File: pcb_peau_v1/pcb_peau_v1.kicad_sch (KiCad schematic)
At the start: 23 parts, among them J1 Conn_01x05, J2 Conn_01x05, J3 Conn_01x16, J4 Conn_01x24, U1 REF200AU, U2 TLC274, U3 CD74HC4067SM, U4 CD74HC4067SM, U5 CD74HC4067SM, U6 CD74HC4067SM, U7 TLC274, U8 TLC274, U9 TLC274

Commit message: Schématic
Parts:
- added H1, H2, H3, H4: MountingHole_Pad, MountingHole:MountingHole_3.2mm_M3_DIN965_Pad, symbol Mechanical:MountingHole_Pad
- J1, J2: footprint (none) -> Connector_JST:JST_EH_B5B-EH-A_1x05_P2.50mm_Vertical
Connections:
- net 0: now also H1.1, H2.1, H3.1, H4.1
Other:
- title: (none) -> PCB PEAU
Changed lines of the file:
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@@
 (kicad_sch (version 20230121) (generator eeschema)
   (paper "A3")
+  (title_block
+    (title "PCB PEAU")
+    (date "2023-11-14")
+    (rev "1.0")
+  )
   (junction (at 88.9 129.54) (diameter 0) (color 0 0 0 0)
   )
@@
   (junction (at 116.84 241.3) (diameter 0) (color 0 0 0 0)
   )
+  (junction (at 172.72 39.37) (diameter 0) (color 0 0 0 0)
+  )
   (junction (at 109.22 237.49) (diameter 0) (color 0 0 0 0)
   )
@@
   (junction (at 246.38 243.84) (diameter 0) (color 0 0 0 0)
   )
+  (junction (at 172.72 45.72) (diameter 0) (color 0 0 0 0)
+  )
   (junction (at 124.46 147.32) (diameter 0) (color 0 0 0 0)
   )
@@
   )
   (junction (at 40.64 129.54) (diameter 0) (color 0 0 0 0)
+  )
+  (junction (at 172.72 33.02) (diameter 0) (color 0 0 0 0)
   )
   (junction (at 116.84 143.51) (diameter 0) (color 0 0 0 0)
@@
     (stroke (width 0) (type default))
   )
+  (polyline (pts (xy 201.93 55.88) (xy 163.83 55.88))
+    (stroke (width 0) (type default))
+  )
   (wire (pts (xy 104.14 137.16) (xy 104.14 234.95))
     (stroke (width 0) (type default))
@@
     (stroke (width 0) (type default))
   )
+  (wire (pts (xy 172.72 33.02) (xy 172.72 39.37))
+    (stroke (width 0) (type default))
+  )
   (wire (pts (xy 215.9 220.98) (xy 215.9 212.09))
     (stroke (width 0) (type default))
@@
     (stroke (width 0) (type default))
   )
+  (wire (pts (xy 172.72 26.67) (xy 172.72 33.02))
+    (stroke (width 0) (type default))
+  )
   (wire (pts (xy 93.98 229.87) (xy 93.98 247.65))
     (stroke (width 0) (type default))
@@
     (stroke (width 0) (type default))
   )
+  (wire (pts (xy 172.72 45.72) (xy 172.72 52.07))
+    (stroke (width 0) (type default))
+  )
+  (wire (pts (xy 172.72 39.37) (xy 172.72 45.72))
+    (stroke (width 0) (type default))
+  )
   (polyline (pts (xy 144.78 21.59) (xy 22.86 21.59))
     (stroke (width 0) (type default))
@@
     (stroke (width 0) (type default))
   )
+  (polyline (pts (xy 201.93 21.59) (xy 201.93 55.88))
+    (stroke (width 0) (type default))
+  )
   (wire (pts (xy 148.59 226.06) (xy 148.59 231.14))
     (stroke (width 0) (type default))
@@
     (stroke (width 0) (type default))
   )
+  (polyline (pts (xy 163.83 21.59) (xy 201.93 21.59))
+    (stroke (width 0) (type default))
+  )
   (wire (pts (xy 260.35 229.87) (xy 260.35 226.06))
     (stroke (width 0) (type default))
@@
   )
   (polyline (pts (xy 22.86 21.59) (xy 22.86 26.67))
+    (stroke (width 0) (type default))
+  )
+  (polyline (pts (xy 163.83 21.59) (xy 163.83 55.88))
     (stroke (width 0) (type default))
   )
@@
     (property "Intersheetrefs" "${INTERSHEET_REFS}" (at 156.21 98.9361 90)
       (effects (font (size 1.27 1.27)) (justify left) hide)
+    )
+  )
+  (symbol (lib_id "Mechanical:MountingHole_Pad") (at 175.26 26.67 270) (unit 1)
+    (in_bom yes) (on_board yes) (dnp no) (fields_autoplaced)
+    (property "Reference" "H1" (at 179.07 26.035 90)
+      (effects (font (size 1.27 1.27)) (justify left))
+    )
+    (property "Value" "MountingHole_Pad" (at 179.07 28.575 90)
+      (effects (font (size 1.27 1.27)) (justify left))
+    )
+    (property "Footprint" "MountingHole:MountingHole_3.2mm_M3_DIN965_Pad" (at 175.26 26.67 0)
+      (effects (font (size 1.27 1.27)) hide)
+    )
+    (property "Datasheet" "~" (at 175.26 26.67 0)
+      (effects (font (size 1.27 1.27)) hide)
+    )
+    (pin "1")
+    (instances
+      (project "pcb_peau_v1"
+        (path "/819805aa-dc61-4334-bd44-f4820d1efad6"
+          (reference "H1") (unit 1)
+        )
+      )
     )
   )
@@
     )
   )
+  (symbol (lib_id "Mechanical:MountingHole_Pad") (at 175.26 39.37 270) (unit 1)
+    (in_bom yes) (on_board yes) (dnp no) (fields_autoplaced)
+    (property "Reference" "H3" (at 179.07 38.735 90)
+      (effects (font (size 1.27 1.27)) (justify left))
+    )
+    (property "Value" "MountingHole_Pad" (at 179.07 41.275 90)
+      (effects (font (size 1.27 1.27)) (justify left))
+    )
+    (property "Footprint" "MountingHole:MountingHole_3.2mm_M3_DIN965_Pad" (at 175.26 39.37 0)
+      (effects (font (size 1.27 1.27)) hide)
+    )
+    (property "Datasheet" "~" (at 175.26 39.37 0)
+      (effects (font (size 1.27 1.27)) hide)
+    )
+    (pin "1")
+    (instances
+      (project "pcb_peau_v1"
+        (path "/819805aa-dc61-4334-bd44-f4820d1efad6"
+          (reference "H3") (unit 1)
+        )
+      )
+    )
+  )
+  (symbol (lib_id "Mechanical:MountingHole_Pad") (at 175.26 45.72 270) (unit 1)
+    (in_bom yes) (on_board yes) (dnp no) (fields_autoplaced)
+    (property "Reference" "H4" (at 179.07 45.085 90)
+      (effects (font (size 1.27 1.27)) (justify left))
+    )
+    (property "Value" "MountingHole_Pad" (at 179.07 47.625 90)
+      (effects (font (size 1.27 1.27)) (justify left))
+    )
+    (property "Footprint" "MountingHole:MountingHole_3.2mm_M3_DIN965_Pad" (at 175.26 45.72 0)
+      (effects (font (size 1.27 1.27)) hide)
+    )
+    (property "Datasheet" "~" (at 175.26 45.72 0)
+      (effects (font (size 1.27 1.27)) hide)
+    )
+    (pin "1")
+    (instances
+      (project "pcb_peau_v1"
+        (path "/819805aa-dc61-4334-bd44-f4820d1efad6"
+          (reference "H4") (unit 1)
+        )
+      )
+    )
+  )
   (symbol (lib_id "power:+5V") (at 132.08 116.84 90) (unit 1)
     (in_bom yes) (on_board yes) (dnp no) (fields_autoplaced)
@@
       (effects (font (size 1.27 1.27)) (justify left))
     )
-    (property "Footprint" "" (at 124.46 34.29 0)
+    (property "Footprint" "Connector_JST:JST_EH_B5B-EH-A_1x05_P2.50mm_Vertical" (at 124.46 34.29 0)
       (effects (font (size 1.27 1.27)) hide)
     )
@@
     )
   )
+  (symbol (lib_id "Mechanical:MountingHole_Pad") (at 175.26 33.02 270) (unit 1)
+    (in_bom yes) (on_board yes) (dnp no) (fields_autoplaced)
+    (property "Reference" "H2" (at 179.07 32.385 90)
+      (effects (font (size 1.27 1.27)) (justify left))
+    )
+    (property "Value" "MountingHole_Pad" (at 179.07 34.925 90)
+      (effects (font (size 1.27 1.27)) (justify left))
+    )
+    (property "Footprint" "MountingHole:MountingHole_3.2mm_M3_DIN965_Pad" (at 175.26 33.02 0)
+      (effects (font (size 1.27 1.27)) hide)
+    )
+    (property "Datasheet" "~" (at 175.26 33.02 0)
+      (effects (font (size 1.27 1.27)) hide)
+    )
+    (pin "1")
+    (instances
+      (project "pcb_peau_v1"
+        (path "/819805aa-dc61-4334-bd44-f4820d1efad6"
+          (reference "H2") (unit 1)
+        )
+      )
+    )
+  )
   (symbol (lib_id "Connector_Generic:Conn_01x16") (at 104.14 252.73 90) (mirror x) (unit 1)
     (in_bom yes) (on_board yes) (dnp no)
@@
         (path "/819805aa-dc61-4334-bd44-f4820d1efad6"
           (reference "#PWR07") (unit 1)
+        )
+      )
+    )
+  )
+  (symbol (lib_id "Simulation_SPICE:0") (at 172.72 52.07 0) (unit 1)
+    (in_bom yes) (on_board yes) (dnp no) (fields_autoplaced)
+    (property "Reference" "#GND012" (at 172.72 54.61 0)
+      (effects (font (size 1.27 1.27)) hide)
+    )
+    (property "Value" "0" (at 172.72 50.8 0)
+      (effects (font (size 1.27 1.27)))
+    )
+    (property "Footprint" "" (at 172.72 52.07 0)
+      (effects (font (size 1.27 1.27)) hide)
+    )
+    (property "Datasheet" "~" (at 172.72 52.07 0)
+      (effects (font (size 1.27 1.27)) hide)
+    )
+    (pin "1")
+    (instances
+      (project "pcb_peau_v1"
+        (path "/819805aa-dc61-4334-bd44-f4820d1efad6"
+          (reference "#GND012") (unit 1)
         )
       )
@@
       (effects (font (size 1.27 1.27)) (justify left))
     )
-    (property "Footprint" "" (at 111.76 58.42 0)
-      (effects (font (size 1.27 1.27)) hide)
-    )
+    (property "Footprint" "Connector_JST:JST_EH_B5B-EH-A_1x05_P2.50mm_Vertical" (at 111.76 58.42 0)
+      (effects (font (size 1.27 1.27)) hide)
+    )

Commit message: PCB footprints en cours
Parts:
- removed J3: Conn_01x16, symbol Connector_Generic:Conn_01x16
- removed J4: Conn_01x24, symbol Connector_Generic:Conn_01x24
- added J4: Conn_02x08_Top_Bottom, Connector_JST:JST_PHD_B16B-PHDSS_2x08_P2.00mm_Vertical, symbol Connector_Generic:Conn_02x08_Top_Bottom
- added J5: Conn_02x12_Top_Bottom, Connector_JST:JST_PHD_B24B-PHDSS_2x12_P2.00mm_Vertical, symbol Connector_Generic:Conn_02x12_Top_Bottom
- added unit 5 of U2
- added unit 5 of U7
- added unit 5 of U8
- added unit 5 of U9
- H1: footprint MountingHole:MountingHole_3.2mm_M3_DIN965_Pad -> Resistor_SMD:R_0603_1608Metric_Pad0.98x0.95mm_HandSolder
- R10, R11, R20, R21, R22, R23, R25, R4, R8, R9: footprint (none) -> Resistor_SMD:R_0603_1608Metric_Pad0.98x0.95mm_HandSolder
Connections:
- net +5V: now also U2.4 (V+), U7.4 (V+), U8.4 (V+), U9.4 (V+)
- net 0: now also J5.23 (Pin_23), J5.24 (Pin_24); no longer U3.1 (COM), U5.1 (COM)
- net A1: now also J5.2 (Pin_2)
- net A2: now also J5.18 (Pin_18)
- net AOP0IN+: now also J2.2 (Pin_2); no longer J2.1 (Pin_1)
- net B1: now also J5.3 (Pin_3)
- net B2: now also J5.19 (Pin_19)
- net C1: now also J5.4 (Pin_4)
- net C2: now also J5.20 (Pin_20)
- net D1: now also J5.5 (Pin_5)
- net D2: now also J5.21 (Pin_21)
- net NE1: now also J5.6 (Pin_6)
- net NE2: now also J5.17 (Pin_17)
- net TRIOAOP1: now also J5.22 (Pin_22)
- net U1C2: no longer J2.3 (Pin_3)
- net at U3.16 (I15), U4.16 (I15), U5.9 (I0)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: now also J4.1 (Pin_1); no longer U5.16 (I15), U6.16 (I15)
- net at U3.17 (I14), U4.17 (I14): now also U5.16 (I15), U6.16 (I15), J4.16 (Pin_16); no longer U5.17 (I14), U6.17 (I14)
- net at U3.18 (I13), U4.18 (I13): now also U5.17 (I14), U6.17 (I14), J4.15 (Pin_15); no longer U5.18 (I13), U6.18 (I13)
- net at U3.19 (I12), U4.19 (I12): now also U5.18 (I13), U6.18 (I13), J4.14 (Pin_14); no longer U5.19 (I12), U6.19 (I12)
- net at U3.2 (I7), U4.2 (I7): now also U5.23 (I8), U6.23 (I8), J4.9 (Pin_9); no longer U5.2 (I7), U6.2 (I7)
- net at U3.20 (I11), U4.20 (I11): now also U5.19 (I12), U6.19 (I12), J4.13 (Pin_13); no longer U5.20 (I11), U6.20 (I11)
- net at U3.21 (I10), U4.21 (I10): now also U5.20 (I11), U6.20 (I11), J4.12 (Pin_12); no longer U5.21 (I10), U6.21 (I10)
- net at U3.22 (I9), U4.22 (I9): now also U5.21 (I10), U6.21 (I10), J4.11 (Pin_11); no longer U5.22 (I9), U6.22 (I9)
- net at U3.23 (I8), U4.23 (I8): now also U5.22 (I9), U6.22 (I9), J4.10 (Pin_10); no longer U5.23 (I8), U6.23 (I8)
- net at U3.3 (I6), U4.3 (I6): now also U5.2 (I7), U6.2 (I7), J4.8 (Pin_8); no longer U5.3 (I6), U6.3 (I6)
- net at U3.4 (I5), U4.4 (I5): now also U5.3 (I6), U6.3 (I6), J4.7 (Pin_7); no longer U5.4 (I5), U6.4 (I5)
- net at U3.5 (I4), U4.5 (I4): now also U5.4 (I5), U6.4 (I5), J4.6 (Pin_6); no longer U5.5 (I4), U6.5 (I4)
- net at U3.6 (I3), U4.6 (I3): now also U5.5 (I4), U6.5 (I4), J4.5 (Pin_5); no longer U5.6 (I3), U6.6 (I3)
- net at U3.7 (I2), U4.7 (I2): now also U5.6 (I3), U6.6 (I3), J4.4 (Pin_4); no longer U5.7 (I2), U6.7 (I2)
- net at U3.9 (I0), U4.9 (I0), U5.8 (I1)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: now also J4.2 (Pin_2); no longer U3.8 (I1)
- net at U4.8 (I1): now also U3.8 (I1), U5.7 (I2), U6.7 (I2), J4.3 (Pin_3)
- new net -5V: U2.11 (V-), U7.11 (V-), U8.11 (V-), U9.11 (V-)
- new net 1-ENTREE: J2.1 (Pin_1), U5.1 (COM)
- new net 2-ENTREE: J2.3 (Pin_3), U3.1 (COM)
- no-connect marks 3 -> 15
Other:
- moved on the sheet: U1C, U3, U5, U6

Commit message: Début du PCB
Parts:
- U2, U7, U8, U9: footprint (none) -> CUSTOM:SO14
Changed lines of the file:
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@@
       (effects (font (size 1.27 1.27)) (justify right))
     )
-    (property "Footprint" "" (at 257.81 255.27 0)
+    (property "Footprint" "CUSTOM:SO14" (at 257.81 255.27 0)
       (effects (font (size 1.27 1.27)) hide)
     )
@@
       (effects (font (size 1.27 1.27)) hide)
     )
-    (property "Footprint" "" (at 226.06 147.32 0)
+    (property "Footprint" "CUSTOM:SO14" (at 226.06 147.32 0)
       (effects (font (size 1.27 1.27)) hide)
     )
@@
       (effects (font (size 1.27 1.27)) (justify right))
     )
-    (property "Footprint" "" (at 224.79 147.32 0)
+    (property "Footprint" "CUSTOM:SO14" (at 224.79 147.32 0)
       (effects (font (size 1.27 1.27)) hide)
     )
@@
       (effects (font (size 1.27 1.27)) hide)
     )
-    (property "Footprint" "" (at 259.08 255.27 0)
+    (property "Footprint" "CUSTOM:SO14" (at 259.08 255.27 0)
       (effects (font (size 1.27 1.27)) hide)
     )
@@
       (effects (font (size 1.27 1.27)) (justify right))
     )
-    (property "Footprint" "" (at 236.22 223.52 0)
+    (property "Footprint" "CUSTOM:SO14" (at 236.22 223.52 0)
       (effects (font (size 1.27 1.27)) hide)
     )
@@
       (effects (font (size 1.27 1.27)) hide)
     )
-    (property "Footprint" "" (at 227.33 255.27 0)
+    (property "Footprint" "CUSTOM:SO14" (at 227.33 255.27 0)
       (effects (font (size 1.27 1.27)) hide)
     )
@@
       (effects (font (size 1.27 1.27)))
     )
-    (property "Footprint" "" (at 236.22 223.52 0)
+    (property "Footprint" "CUSTOM:SO14" (at 236.22 223.52 0)
       (effects (font (size 1.27 1.27)) hide)
     )
@@
       (effects (font (size 1.27 1.27)) (justify right))
     )
-    (property "Footprint" "" (at 227.33 255.27 0)
-      (effects (font (size 1.27 1.27)) hide)
-    )
+    (property "Footprint" "CUSTOM:SO14" (at 227.33 255.27 0)
+      (effects (font (size 1.27 1.27)) hide)
+    )

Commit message: PCB début
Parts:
- H1: footprint Resistor_SMD:R_0603_1608Metric_Pad0.98x0.95mm_HandSolder -> MountingHole:MountingHole_3.2mm_M3_DIN965_Pad

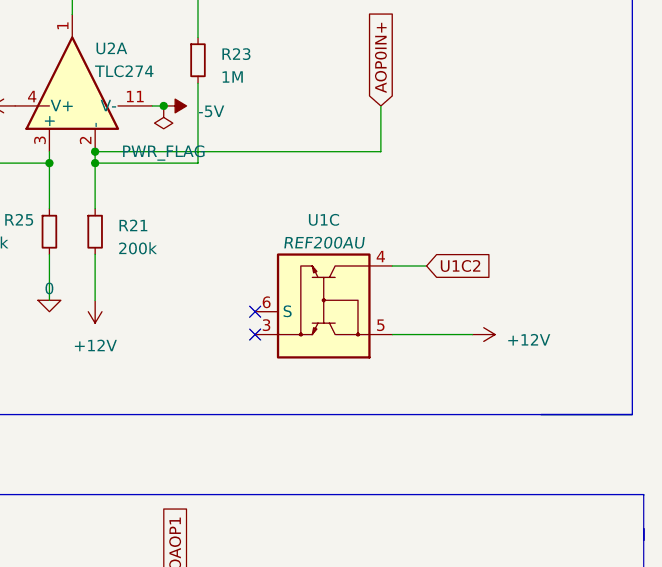
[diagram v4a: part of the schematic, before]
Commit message: PCB Mux/demux
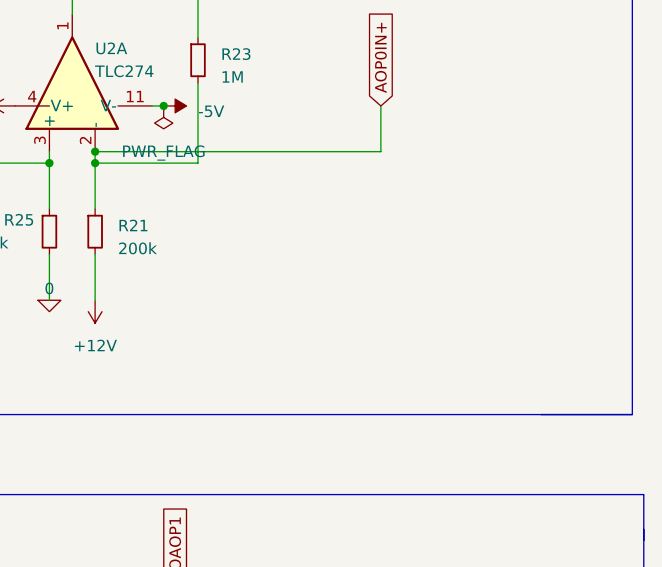
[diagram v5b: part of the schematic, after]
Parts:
- removed U1: REF200AU, Package_SO:SOIC-8_3.9x4.9mm_P1.27mm, symbol Reference_Current:REF200AU
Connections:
- no-connect marks 15 -> 13
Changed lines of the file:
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@@
   )
   (no_connect (at 64.77 40.64))
-  (no_connect (at 247.65 173.99))
   (no_connect (at 52.07 60.96))
   (no_connect (at 52.07 35.56))
@@
   (no_connect (at 64.77 43.18))
   (no_connect (at 52.07 63.5))
-  (no_connect (at 247.65 171.45))
   (wire (pts (xy 96.52 133.35) (xy 96.52 214.63))
     (stroke (width 0) (type default))
@@
     (stroke (width 0) (type default))
   )
-  (wire (pts (xy 262.89 173.99) (xy 271.78 173.99))
-    (stroke (width 0) (type default))
-  )
   (wire (pts (xy 173.99 101.6) (xy 173.99 104.14))
     (stroke (width 0) (type default))
@@
   )
   (wire (pts (xy 45.72 228.6) (xy 45.72 213.36))
-    (stroke (width 0) (type default))
-  )
-  (wire (pts (xy 266.7 166.37) (xy 262.89 166.37))
     (stroke (width 0) (type default))
   )
@@
     (effects (font (size 1.27 1.27)) (justify left))
     (property "Intersheetrefs" "${INTERSHEET_REFS}" (at 261.62 137.2779 90)
-      (effects (font (size 1.27 1.27)) (justify left) hide)
-    )
-  )
-  (global_label "U1C2" (shape input) (at 266.7 166.37 0) (fields_autoplaced)
-    (effects (font (size 1.27 1.27)) (justify left))
-    (property "Intersheetrefs" "${INTERSHEET_REFS}" (at 274.6253 166.37 0)
       (effects (font (size 1.27 1.27)) (justify left) hide)
     )
@@
     )
   )
-  (symbol (lib_id "power:+12V") (at 271.78 173.99 270) (unit 1)
-    (in_bom yes) (on_board yes) (dnp no) (fields_autoplaced)
-    (property "Reference" "#PWR02" (at 267.97 173.99 0)
-      (effects (font (size 1.27 1.27)) hide)
-    )
-    (property "Value" "+12V" (at 275.59 174.625 90)
-      (effects (font (size 1.27 1.27)) (justify left))
-    )
-    (property "Footprint" "" (at 271.78 173.99 0)
-      (effects (font (size 1.27 1.27)) hide)
-    )
-    (property "Datasheet" "" (at 271.78 173.99 0)
-      (effects (font (size 1.27 1.27)) hide)
-    )
-    (pin "1")
-    (instances
-      (project "pcb_peau_v1"
-        (path "/819805aa-dc61-4334-bd44-f4820d1efad6"
-          (reference "#PWR02") (unit 1)
-        )
-      )
-    )
-  )
   (symbol (lib_id "Device:R_Small") (at 213.36 143.51 0) (unit 1)
     (in_bom yes) (on_board yes) (dnp no) (fields_autoplaced)
@@
         )
       )
-    )
-  )
-  (symbol (lib_id "Reference_Current:REF200AU") (at 255.27 173.99 270) (mirror x) (unit 3)
-    (in_bom yes) (on_board yes) (dnp no) (fields_autoplaced)
-    (property "Reference" "U1" (at 255.27 161.29 90)
-      (effects (font (size 1.27 1.27)))
-    )
-    (property "Value" "REF200AU" (at 255.27 163.83 90)
-      (effects (font (size 1.27 1.27) italic))
-    )
-    (property "Footprint" "Package_SO:SOIC-8_3.9x4.9mm_P1.27mm" (at 255.905 177.165 0)
-      (effects (font (size 1.27 1.27) italic) (justify right) hide)
-    )
-    (property "Datasheet" "www.ti.com/lit/ds/symlink/ref200.pdf" (at 255.27 166.37 0)
-      (effects (font (size 1.27 1.27) italic) hide)
-    )
-    (pin "6")
-    (pin "1")
-    (pin "8")
-    (pin "2")
-    (pin "7")
-    (pin "3")
-    (pin "4")
-    (pin "5")
-    (instances
-      (project "pcb_peau_v1"
-        (path "/819805aa-dc61-4334-bd44-f4820d1efad6"
-          (reference "U1") (unit 3)
-        )
-      )
